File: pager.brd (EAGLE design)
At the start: 78.4 x 44.8 mm, 62 parts, among them Q1 25 MHz, Q2 SI2333DS, SW1 CHS-01A1, SW2 CHS-01A1, U1 VOCORE2SMD, U2 VOCORE2SMD, U3 XR22800IL, X1 52745-3090

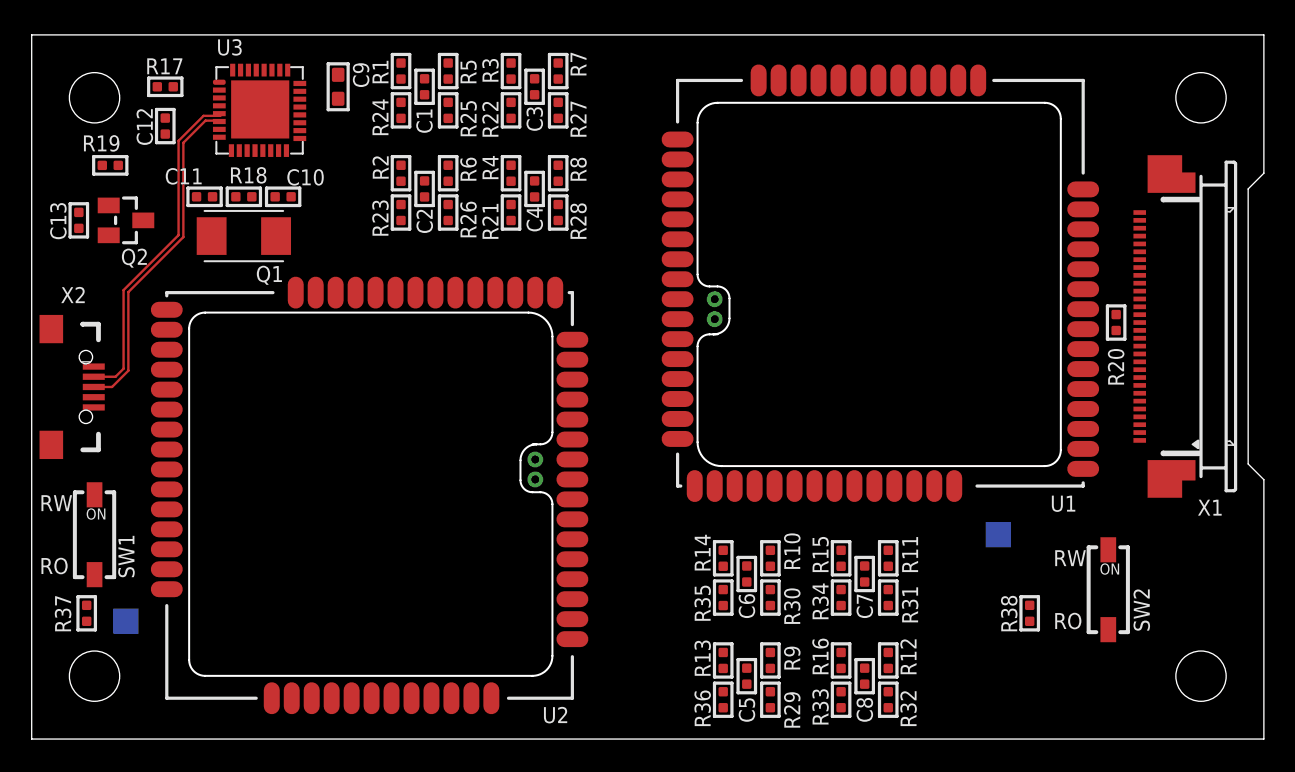
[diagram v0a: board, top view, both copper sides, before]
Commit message: trying to route
Will be ripped up, just to see
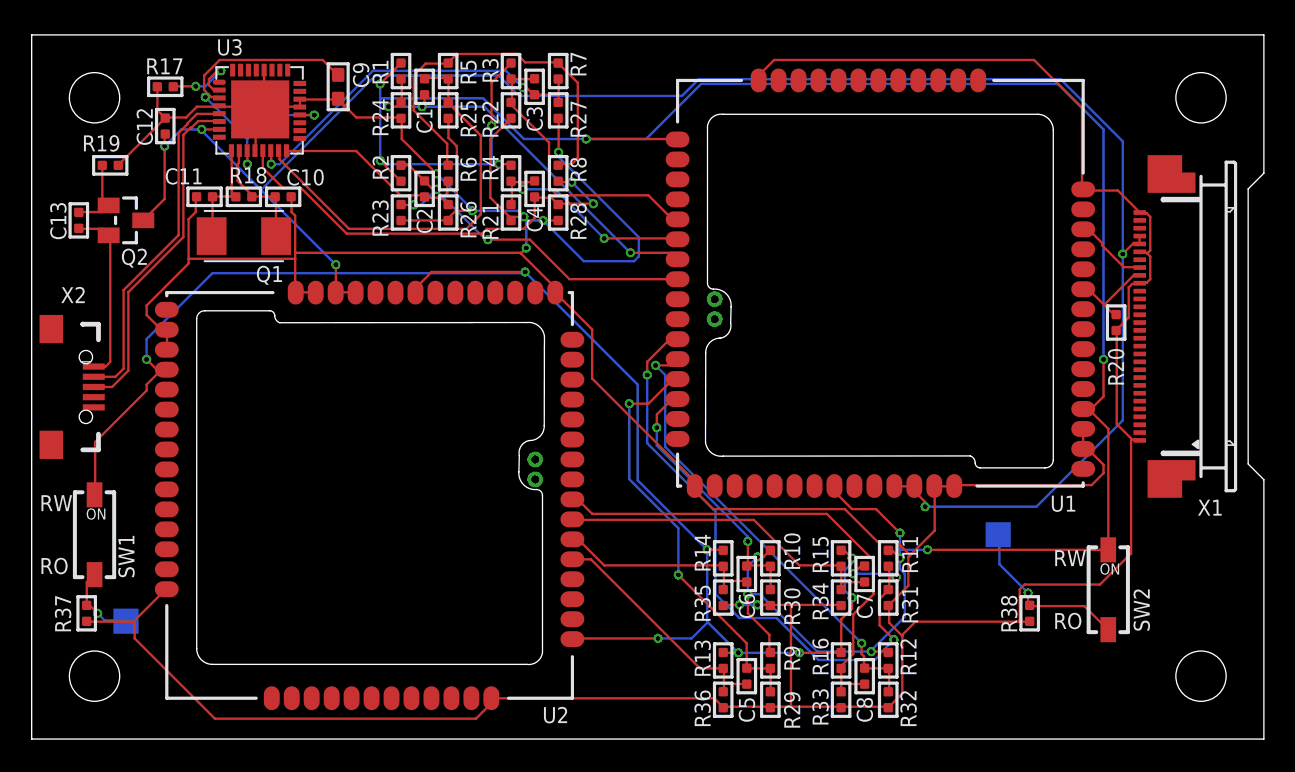
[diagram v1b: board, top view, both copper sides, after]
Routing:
- net GND: track 0.00 -> 337.2 mm, vias 0 -> 8
- net 3.3_CORE: track 0.00 -> 154.9 mm, vias 0 -> 12
- net +5V: track 0.00 -> 123.1 mm, vias 0 -> 5
- net 3.3_WIFI: track 0.00 -> 101.6 mm, vias 0 -> 8
- net ETH_2A_RX_P: track 0.00 -> 42.4 mm, vias 0 -> 4
- net ETH_2B_TX_N: track 0.00 -> 31.5 mm
- net ETH_2A_RX_N: track 0.00 -> 29.4 mm, vias 0 -> 2
- net ETH_1B_TX_N: track 0.00 -> 28.7 mm, vias 0 -> 2
- net ETH_1B_RX_P: track 0.00 -> 26.7 mm
- net ETH_2A_TX_P: track 0.00 -> 26.6 mm, vias 0 -> 2
- net ETH_1A_TX_P: track 0.00 -> 25.7 mm, vias 0 -> 3
- net N$10: track 0.00 -> 24.6 mm
- net ETH_1B_TX_P: track 0.00 -> 23.8 mm, vias 0 -> 2
- net BIAS_1B: track 0.00 -> 23.8 mm, vias 0 -> 3
- net ETH_1A_TX_N: track 0.00 -> 23.3 mm, vias 0 -> 3
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
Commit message: Fixed some parts, better placement
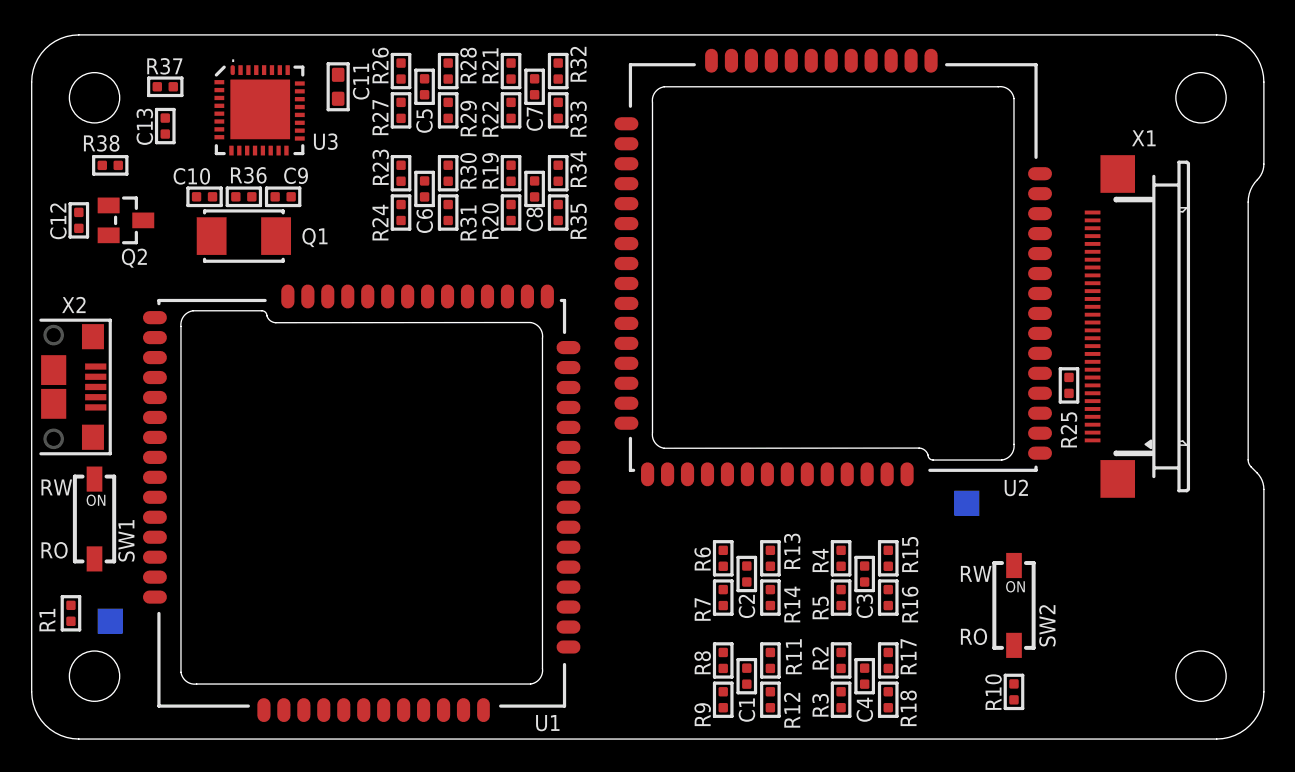
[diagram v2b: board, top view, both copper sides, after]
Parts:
- removed WP_CORE, WP_WIFI: TPTP16SQ, pager:TP16SQ
- added TP1, TP2: TPTP16SQ, pager:TP16SQ
- C11: value 18 pF -> 4.7 uF cer; device pager:_0402 -> pager:_0603
- C9: value 4.7 uF cer -> 18 pF; device pager:_0603 -> pager:_0402
- R1, R10, R25: value 50 -> 10 k
- R17: value 226 -> 50
- R18: value 1M -> 50
- R19: value 40.2k -> 50
- R20: value 10 k -> 50
- R36: value 50 -> 1M
- R37: value 10 k -> 226
- R38: value 10 k -> 40.2k
- U1, U2: value VOCORE2SMD -> VOCORE2-SMD
- X1: value 52745-3090 -> OMRON_XF2L-30REVERSE; device pager:52745-3090 -> pager:OMRON_XF2L-30
- X2: value (none) -> FCI_8193_MICRO_USB; device pager:USB-MICRO-SMD -> pager:FCI_MICRO_USB_8193
- moved R38 65.1 mm to (5.00, 36.5), turned to 180 degrees
- moved R17 58.7 mm to (54.5, 5.00), turned to 90 degrees
- moved R18 52.0 mm to (54.5, 2.50), turned to 90 degrees
- moved R3 45.2 mm to (51.5, 2.50)
- moved R32 45.2 mm to (33.5, 42.5)
- moved R36 44.2 mm to (13.5, 34.5), turned to 180 degrees
- moved R25 43.2 mm to (66.0, 22.5)
- moved C1 42.7 mm to (45.5, 4.00), turned to 270 degrees
- moved C5 42.7 mm to (25.0, 41.5), turned to 90 degrees
- moved R29 42.7 mm to (26.5, 40.0)
- moved R5 41.8 mm to (51.5, 9.00)
- moved R2 41.8 mm to (51.5, 5.00), turned to 90 degrees
- moved R33 41.6 mm to (33.5, 40.0)
- moved R1 40.4 mm to (2.50, 8.00)
- moved R20 39.1 mm to (30.5, 33.5)
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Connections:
- removed net BIAS_1B: C9.1, U3.11, U3.20, U3.3
- removed net N$26: X2.GND1
- new net 3.3V_USB: C11.1, U3.13, U3.22, U3.30
- net +5V: now also C13.1, U3.26, X1.4, X1.5; no longer C12.1, U3.7, X1.26, X1.27
- net 3.3_CORE: now also R13.2, R15.2, R17.2, R19.2, R21.2, R23.2, R26.2, U2.PB07, U2.PL00, U2.PR11; no longer R1.2, R10.2, R12.2, R2.2, R3.2, R4.2, R9.2, U1.PB07, U1.PL00, U1.PR11
- net 3.3_WIFI: now also R2.2, R4.2, R6.2, R8.2, U1.PB07, U1.PL00, U1.PR11; no longer R13.2, R14.2, R15.2, R16.2, U2.PB07, U2.PL00, U2.PR11
- net DISP_RESET: now also R25.2, U2.PR05, X1.9; no longer R20.2, U1.PR05, X1.22
- net DISP_RX0: now also U2.PR02, X1.8; no longer U1.PR02, X1.23
- net DISP_TX0: now also U2.PR01, X1.7; no longer U1.PR01, X1.24
- net ETH_1A_RX_N: now also C8.1, R19.1, R20.2, U2.PL05; no longer C4.1, R21.2, R4.1, U1.PL05
- net ETH_1A_RX_P: now also C7.1, R21.1, U2.PL04; no longer C3.1, R3.1, U1.PL04
- net ETH_1A_TX_N: now also C6.1, R23.1, R24.2, U2.PL07; no longer C2.1, R2.1, R23.2, U1.PL07
- net ETH_1A_TX_P: now also C5.1, R26.1, R27.2, U2.PL06; no longer C1.1, R1.1, R24.2, U1.PL06
- net ETH_1B_RX_N: now also C6.2, R30.1, R31.2, U3.17; no longer C2.2, R26.2, R6.1, U3.16
- net ETH_1B_RX_P: now also C5.2, R28.1, R29.2, U3.18; no longer C1.2, R25.2, R5.1, U3.15
- net ETH_1B_TX_N: now also C8.2, R34.1, R35.2, U3.20; no longer C4.2, R28.2, R8.1, U3.13
- net ETH_1B_TX_P: now also C7.2, R32.1, R33.2, U3.19; no longer C3.2, R27.2, R7.1, U3.14
- net ETH_2A_RX_N: now also C4.1, R17.1, R18.2, U2.PL11; no longer C8.1, R12.1, R32.2, U1.PL11
- net ETH_2A_RX_P: now also C3.1, R15.1, R16.2, U2.PL10; no longer C7.1, R11.1, R31.2, U1.PL10
- net ETH_2A_TX_N: now also C2.1, R13.1, R14.2, U2.PL13; no longer C6.1, R10.1, R30.2, U1.PL13
- net ETH_2A_TX_P: now also C1.1, R11.1, R12.2, U2.PL12; no longer C5.1, R29.2, R9.1, U1.PL12
- net ETH_2B_RX_N: now also C2.2, R6.1, R7.2, U1.PL05; no longer C6.2, R14.1, R35.2, U2.PL05
- net ETH_2B_RX_P: now also C1.2, R8.1, R9.2, U1.PL04; no longer C5.2, R13.1, R36.2, U2.PL04
- net ETH_2B_TX_N: now also C4.2, R2.1, R3.2, U1.PL07; no longer C8.2, R16.1, R33.2, U2.PL07
- net ETH_2B_TX_P: now also C3.2, R4.1, R5.2, U1.PL06; no longer C7.2, R15.1, R34.2, U2.PL06
- net GND: now also C11.2, C13.2, C9.1, R1.1, R10.1, R12.1, R14.1, R16.1, R18.1, R3.1, R5.1, R7.1, R9.1, U3.11, U3.29, U3.5, X1.10, X1.6, X2.GND; no longer C11.1, C12.2, C9.2, R17.1, R19.1, R21.1, R23.1, R26.1, R28.1, R30.1, R32.1, R34.1, R36.1, U3.22, U3.28, U3.4, X1.21, X1.25
- net N$10: now also R28.2, R30.2, R32.2, R34.2; no longer R5.2, R6.2, R7.2, R8.2
- net N$21: now also R37.2, U3.31; no longer R17.2, U3.2
- net N$22: now also C10.2, R36.2, U3.24; no longer C11.2, R18.2, U3.9
- net N$23: now also C9.2, R36.1, U3.23; no longer C10.2, R18.1, U3.10
- net N$27: now also C12.1, X2.VBUS; no longer C13.1, X2.VBUS1
- net N$28: now also C12.2, R38.2; no longer C13.2, R19.2
- net USB_D_N: now also U3.28, X2.D-; no longer U3.5, X2.D-1
- net USB_D_P: now also U3.27, X2.D+; no longer U3.6, X2.D+1
- net WP_CORE: now also R10.2, TP2.TP; no longer R38.2, WP_CORE.TP
- net WP_WIFI: now also R1.2, TP1.TP; no longer R37.2, WP_WIFI.TP
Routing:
- net GND: track 337.2 -> 0.00 mm, vias 8 -> 0
- net 3.3_CORE: track 154.9 -> 0.00 mm, vias 12 -> 0
- net +5V: track 123.1 -> 0.00 mm, vias 5 -> 0
- net 3.3_WIFI: track 101.6 -> 0.00 mm, vias 8 -> 0
- net ETH_2A_RX_P: track 42.4 -> 0.00 mm, vias 4 -> 0
- net ETH_2B_TX_N: track 31.5 -> 0.00 mm
- net ETH_2A_RX_N: track 29.4 -> 0.00 mm, vias 2 -> 0
- net ETH_1B_TX_N: track 28.7 -> 0.00 mm, vias 2 -> 0
- net ETH_1B_RX_P: track 26.7 -> 0.00 mm
- net ETH_2A_TX_P: track 26.6 -> 0.00 mm, vias 2 -> 0
- net ETH_1A_TX_P: track 25.7 -> 0.00 mm, vias 3 -> 0
- net N$10: track 24.6 -> 0.00 mm
- net ETH_1B_TX_P: track 23.8 -> 0.00 mm, vias 2 -> 0
- net BIAS_1B: track 23.8 -> 0.00 mm, vias 3 -> 0
- net ETH_1A_TX_N: track 23.3 -> 0.00 mm, vias 3 -> 0
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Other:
- outline, holes or cut-outs redrawn

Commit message: moved R25 for better prototype soldering access
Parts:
- moved R25 11.2 mm to (72.0, 13.0)
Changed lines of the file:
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@@
 <layer number="17" name="Pads" color="2" fill="1" visible="yes" active="yes"/>
 <layer number="18" name="Vias" color="2" fill="1" visible="yes" active="yes"/>
-<layer number="19" name="Unrouted" color="6" fill="1" visible="no" active="yes"/>
+<layer number="19" name="Unrouted" color="6" fill="1" visible="yes" active="yes"/>
 <layer number="20" name="Dimension" color="15" fill="1" visible="yes" active="yes"/>
 <layer number="21" name="tPlace" color="7" fill="1" visible="yes" active="yes"/>
@@
 <attribute name="VALUE" x="22.1664" y="37.27" size="0.508" layer="27" font="vector" ratio="10" rot="R270"/>
 </element>
-<element name="R25" library="pager" package="_0402" value="10 k" x="66" y="22.5" smashed="yes" rot="R90">
-<attribute name="NAME" x="66.5061" y="18.43" size="1.016" layer="25" font="vector" ratio="14" rot="R90"/>
-<attribute name="VALUE" x="67.3336" y="21.23" size="0.508" layer="27" font="vector" ratio="10" rot="R90"/>
+<element name="R25" library="pager" package="_0402" value="10 k" x="72" y="13" smashed="yes" rot="R90">
+<attribute name="NAME" x="72.5061" y="8.93" size="1.016" layer="25" font="vector" ratio="14" rot="R90"/>
+<attribute name="VALUE" x="73.3336" y="11.73" size="0.508" layer="27" font="vector" ratio="10" rot="R90"/>
 </element>
 <element name="R20" library="pager" package="_0402" value="50" x="30.5" y="33.5" smashed="yes" rot="R90">
@@
 <contactref element="R25" pad="2"/>
 <contactref element="U2" pad="PR05"/>
-<wire x1="66" y1="23.008" x2="67.5" y2="23" width="0" layer="19" extent="1-1"/>
-<wire x1="64.1572" y1="29.619" x2="66" y2="23.008" width="0" layer="19" extent="1-1"/>
+<wire x1="72" y1="13.508" x2="67.5" y2="23" width="0" layer="19" extent="1-1"/>
+<wire x1="64.1572" y1="29.619" x2="72" y2="13.508" width="0" layer="19" extent="1-1"/>
 </signal>
 <signal name="DISP_RX0">
@@
 <contactref element="U2" pad="PT00" route="any" routetag="G$1.GND"/>
 <wire x1="64.1572" y1="35.969" x2="67.5" y2="33.5" width="0" layer="19" extent="1-1"/>
-<wire x1="66" y1="21.992" x2="64.1572" y2="20.729" width="0" layer="19" extent="1-1"/>
-<wire x1="67.5" y1="21.5" x2="66" y2="21.992" width="0" layer="19" extent="1-1"/>
+<wire x1="72" y1="12.492" x2="64.1572" y2="20.729" width="0" layer="19" extent="1-1"/>
+<wire x1="67.5" y1="21.5" x2="72" y2="12.492" width="0" layer="19" extent="1-1"/>
 <wire x1="67.5" y1="23.5" x2="67.5" y2="21.5" width="0" layer="19" extent="1-1"/>
 <wire x1="67.5" y1="19" x2="67.5" y2="21.5" width="0" layer="19" extent="1-1"/>

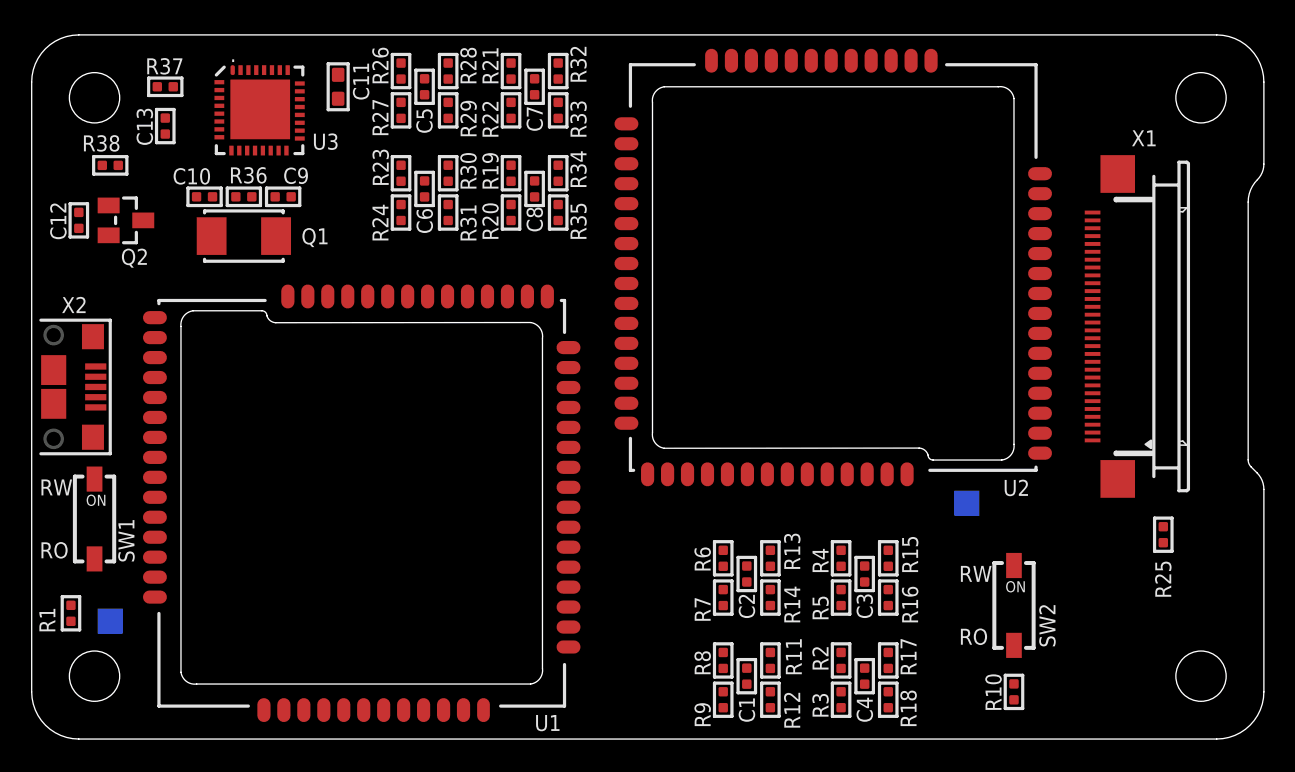
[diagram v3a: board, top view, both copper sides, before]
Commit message: Added wifi_reset wire, polygons on tRestrict for Vocore's and routed power bus and USB
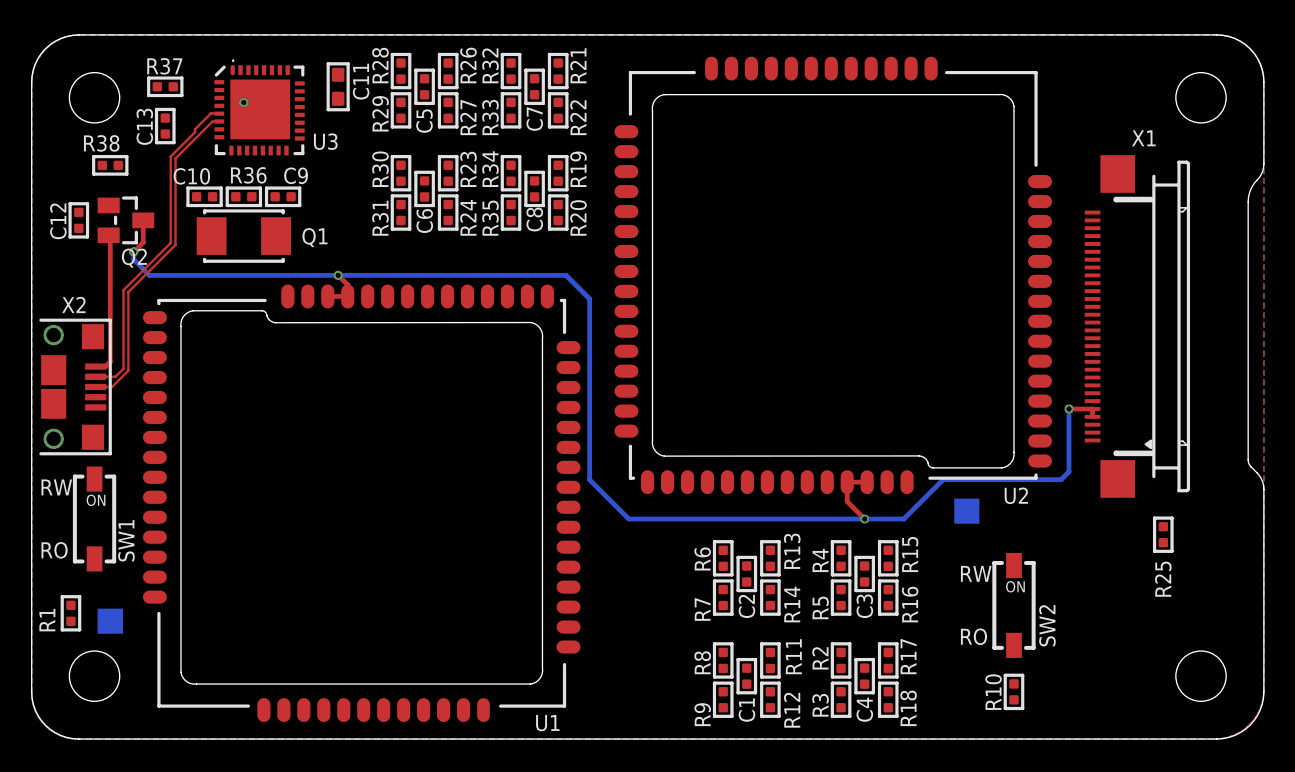
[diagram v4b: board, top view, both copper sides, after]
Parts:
- moved R19 3.00 mm to (33.5, 36.0)
- moved R20 3.00 mm to (33.5, 33.5)
- moved R21 3.00 mm to (33.5, 42.5)
- moved R22 3.00 mm to (33.5, 40.0)
- moved R23 3.00 mm to (26.5, 36.0), turned to 90 degrees
- moved R24 3.00 mm to (26.5, 33.5)
- moved R26 3.00 mm to (26.5, 42.5)
- moved R27 3.00 mm to (26.5, 40.0)
- moved R28 3.00 mm to (23.5, 42.5)
- moved R29 3.00 mm to (23.5, 40.0)
- moved R30 3.00 mm to (23.5, 36.0)
- moved R31 3.00 mm to (23.5, 33.5)
- moved R32 3.00 mm to (30.5, 42.5)
- moved R33 3.00 mm to (30.5, 40.0)
- moved R34 3.00 mm to (30.5, 36.0)
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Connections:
- removed net 3.3V_USB: C11.1, U3.13, U3.22, U3.30
- removed net N$10: R28.2, R30.2, R32.2, R34.2
- new net 3.3_USB: C11.1, R28.2, R30.2, R32.2, R34.2, U3.13, U3.22, U3.30
- new net WIFI_RESET: U1.PR08, U2.PL14
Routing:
- net +5V: track 0.00 -> 90.0 mm, vias 0 -> 4
- net USB_D_N: track 0.00 -> 21.1 mm
- net USB_D_P: track 0.00 -> 21.0 mm
- net N$27: track 0.00 -> 9.14 mm
- added copper zone on layer 1, net GND
- added copper zone on layer 16, net GND

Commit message: Routed
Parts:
- moved R25 6.02 mm to (66.0, 13.5)
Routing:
- net GND: track 0.00 -> 71.6 mm, vias 0 -> 13
- net 3.3_CORE: track 0.00 -> 60.7 mm, vias 0 -> 7
- net 3.3_WIFI: track 0.00 -> 54.9 mm, vias 0 -> 4
- net 3.3_USB: track 0.00 -> 53.3 mm, vias 0 -> 2
- net WIFI_RESET: track 0.00 -> 42.4 mm, vias 0 -> 2
- net ETH_2A_RX_N: track 0.00 -> 38.2 mm, vias 0 -> 2
- net ETH_2A_RX_P: track 0.00 -> 32.6 mm, vias 0 -> 2
- net ETH_2A_TX_P: track 0.00 -> 30.1 mm, vias 0 -> 2
- net ETH_2B_TX_N: track 0.00 -> 30.1 mm, vias 0 -> 2
- net ETH_2B_TX_P: track 0.00 -> 22.8 mm
- net +5V: track 90.0 -> 112.6 mm
- net ETH_2A_TX_N: track 0.00 -> 22.5 mm, vias 0 -> 2
- net ETH_1A_TX_P: track 0.00 -> 21.8 mm
- net ETH_1B_TX_P: track 0.00 -> 21.1 mm, vias 0 -> 2
- net ETH_1B_TX_N: track 0.00 -> 20.4 mm, vias 0 -> 2
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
